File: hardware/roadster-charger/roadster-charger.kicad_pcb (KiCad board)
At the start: 4 copper layers, 74.4 x 50.2 mm, 105 parts, among them J1 USB4505-03-0-A, J2 USB4505-03-0-A, J3 54-00166, Q1 CSD19532Q5B, U1 MPM3606AGQV-P, U10 DAC70501ZDQFT, U12 PI3740-00-LGIZ, U2 ESP32-C3-MINI-1, U3 INA168, U4 OPA340NA, U5 FUSB307BMPX, U6 LM75B, U7 LM5050-1, U8 INA168, U9 OPA340NA

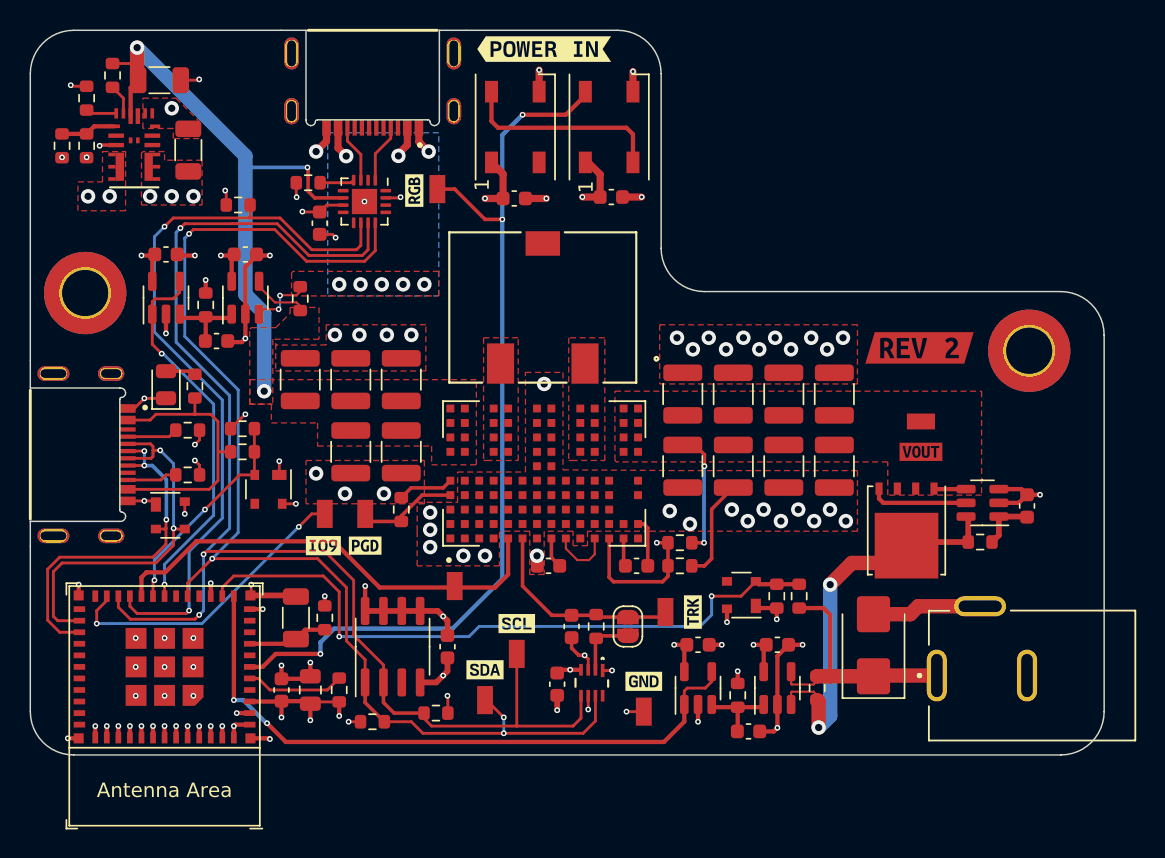
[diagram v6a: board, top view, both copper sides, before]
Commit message: reannotate, add uart test points
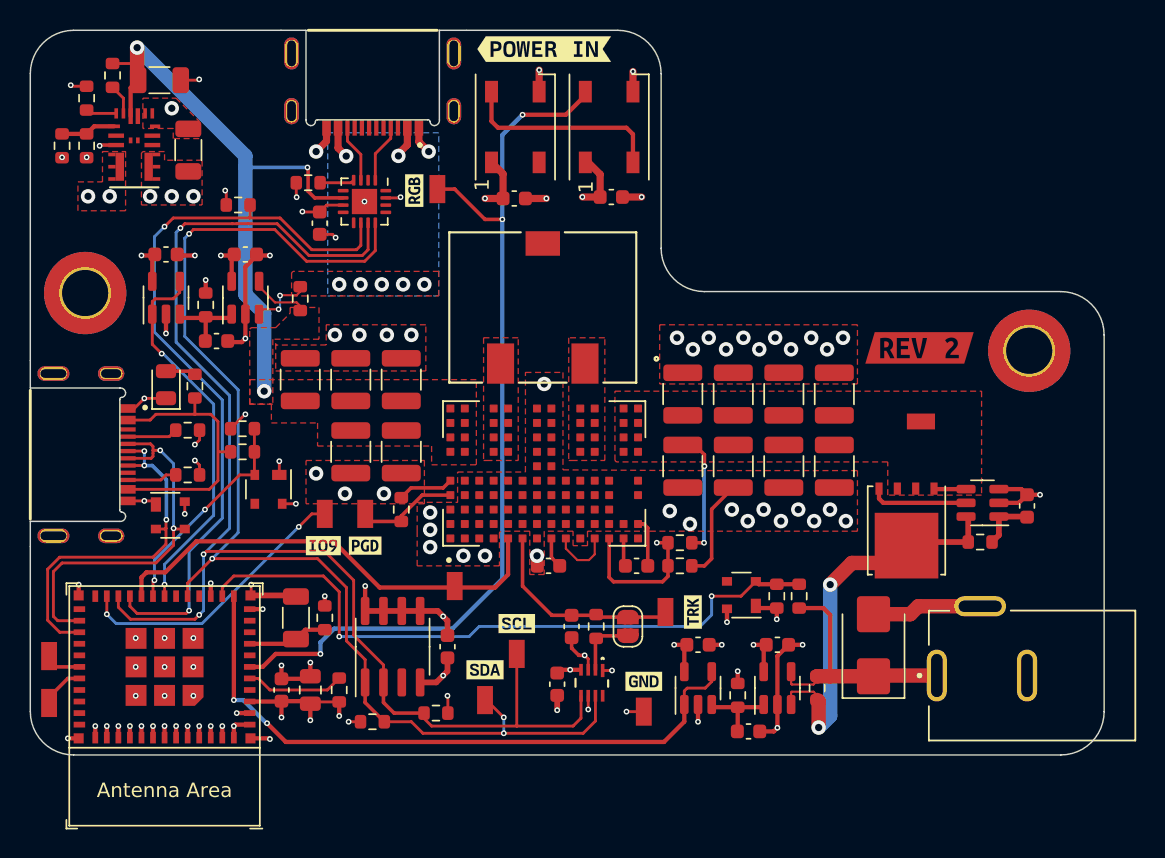
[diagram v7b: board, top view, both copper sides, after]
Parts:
- removed kibuzzard-671EB361: G***, kibuzzard-671EB361
- added TP1: RCU-0C, RCU-0C:TP+195X110, F.Cu at (183.6, 155.9)
- added TP2: RCU-0C, RCU-0C:TP+195X110, F.Cu at (183.6, 152.7)
- added kibuzzard-67218F63: G***, kibuzzard-67218F63, F.Cu at (244.0, 138.5)
- renumbered C25 to C18, C21 to C19, C22 to C20, C23 to C21, C26 to C22, C18 to C23, C20 to C24, C19 to C25, C31 to C26, C32 to C27, C33 to C28, C24 to C29, C27 to C30, C28 to C31, C29 to C32, C30 to C33, D7 to D4, D4 to D5, D5 to D7, R22 to R20, R20 to R21, R21 to R22, R25 to R23, R26 to R25, R23 to R26, TP6 to TP10, TP9 to TP11, TP1 to TP3, TP2 to TP4, TP3 to TP5, TP4 to TP6, TP5 to TP7, TP7 to TP9, U12 to U11
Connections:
- U2 pad 30: unconnected-(U2-GPIO20/U0RXD-Pad30) -> /U0_RX
- U2 pad 31: unconnected-(U2-GPIO21/U0TXD-Pad31) -> /U0_TX
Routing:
- net /U0_TX: track 0.00 -> 3.04 mm
- net /U0_RX: track 0.00 -> 2.67 mm
- net /IO9_BOOT: track 21.1 -> 19.8 mm

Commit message: use track cleanup tool
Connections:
- J1 pad S1: GND -> unconnected-(J1-SHELL_GND-PadS1)_1
- J1 pad S2: GND -> unconnected-(J1-SHELL_GND-PadS1)_3
- J1 pad S3: GND -> unconnected-(J1-SHELL_GND-PadS1)
- J1 pad S4: GND -> unconnected-(J1-SHELL_GND-PadS1)_2
- J2 pad S1: GND -> unconnected-(J2-SHELL_GND-PadS1)_1
- J2 pad S2: GND -> unconnected-(J2-SHELL_GND-PadS1)_2
- J2 pad S3: GND -> unconnected-(J2-SHELL_GND-PadS1)_3
- J2 pad S4: GND -> unconnected-(J2-SHELL_GND-PadS1)
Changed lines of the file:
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@@
 	(net 91 "Net-(U11-VDIFF)")
 	(net 92 "unconnected-(U11-SYNCO-PadC1)")
+	(net 93 "unconnected-(J1-SHELL_GND-PadS1)")
+	(net 94 "unconnected-(J1-SHELL_GND-PadS1)_1")
+	(net 95 "unconnected-(J1-SHELL_GND-PadS1)_2")
+	(net 96 "unconnected-(J1-SHELL_GND-PadS1)_3")
+	(net 97 "unconnected-(J2-SHELL_GND-PadS1)")
+	(net 98 "unconnected-(J2-SHELL_GND-PadS1)_1")
+	(net 99 "unconnected-(J2-SHELL_GND-PadS1)_2")
+	(net 100 "unconnected-(J2-SHELL_GND-PadS1)_3")
 	(footprint "kibuzzard-657BB005"
 		(layer "F.Cu")
@@
 			(layers "*.Cu")
 			(remove_unused_layers no)
-			(net 2 "GND")
+			(net 98 "unconnected-(J2-SHELL_GND-PadS1)_1")
 			(pinfunction "SHELL_GND")
-			(pintype "power_in")
+			(pintype "power_in+no_connect")
 		)
 		(pad "S2" thru_hole oval
@@
 			(layers "*.Cu")
 			(remove_unused_layers no)
-			(net 2 "GND")
+			(net 99 "unconnected-(J2-SHELL_GND-PadS1)_2")
 			(pinfunction "SHELL_GND")
-			(pintype "power_in")
+			(pintype "power_in+no_connect")
 		)
 		(pad "S3" thru_hole oval
@@
 			(layers "*.Cu")
 			(remove_unused_layers no)
-			(net 2 "GND")
+			(net 100 "unconnected-(J2-SHELL_GND-PadS1)_3")
 			(pinfunction "SHELL_GND")
-			(pintype "power_in")
+			(pintype "power_in+no_connect")
 		)
 		(pad "S4" thru_hole oval
@@
 			(layers "*.Cu")
 			(remove_unused_layers no)
-			(net 2 "GND")
+			(net 97 "unconnected-(J2-SHELL_GND-PadS1)")
 			(pinfunction "SHELL_GND")
-			(pintype "power_in")
+			(pintype "power_in+no_connect")
 		)
 		(model "${KIPRJMOD}/components/USB4505-03-0-A_REVA/USB4505-03-0-A_REVA.step"
@@
 			(layers "*.Cu")
 			(remove_unused_layers no)
-			(net 2 "GND")
+			(net 94 "unconnected-(J1-SHELL_GND-PadS1)_1")
 			(pinfunction "SHELL_GND")
-			(pintype "power_in")
+			(pintype "power_in+no_connect")
 		)
 		(pad "S2" thru_hole oval
@@
 			(layers "*.Cu")
 			(remove_unused_layers no)
-			(net 2 "GND")
+			(net 96 "unconnected-(J1-SHELL_GND-PadS1)_3")
 			(pinfunction "SHELL_GND")
-			(pintype "power_in")
+			(pintype "power_in+no_connect")
 		)
 		(pad "S3" thru_hole oval
@@
 			(layers "*.Cu")
 			(remove_unused_layers no)
-			(net 2 "GND")
+			(net 93 "unconnected-(J1-SHELL_GND-PadS1)")
 			(pinfunction "SHELL_GND")
-			(pintype "power_in")
+			(pintype "power_in+no_connect")
 		)
 		(pad "S4" thru_hole oval
@@
 			(layers "*.Cu")
 			(remove_unused_layers no)
-			(net 2 "GND")
+			(net 95 "unconnected-(J1-SHELL_GND-PadS1)_2")
 			(pinfunction "SHELL_GND")
-			(pintype "power_in")
+			(pintype "power_in+no_connect")
 		)
 		(model "${KIPRJMOD}/components/USB4505-03-0-A_REVA/USB4505-03-0-A_REVA.step"
@@
 				(font
 					(size 0.001 0.001)
+					(thickness 0.15)
 				)
 			)
@@
 				(font
 					(size 0.001 0.001)
+					(thickness 0.15)
 				)
 			)
@@
 	)
 	(segment
-		(start 186.75 158.35)
-		(end 186.8 158.3)
-		(width 0.2)
-		(layer "F.Cu")
-		(net 2)
-	)
-	(segment
 		(start 190 158.3)
 		(end 190 157.5)
@@
 	)
 	(segment
-		(start 204.5 157.2)
-		(end 204.45 157.2)
-		(width 0.2)
-		(layer "F.Cu")
-		(net 3)
-	)
-	(segment
 		(start 190 124.9)
 		(end 190.575 124.9)
@@
 	)
 	(segment
-		(start 194.45 130.875)
-		(end 194.425 130.9)
-		(width 0.3)
-		(layer "F.Cu")
-		(net 5)
-	)
-	(segment
 		(start 194.45 129.225)
 		(end 196.0625 129.225)
@@
 	)
 	(segment
-		(start 190.2 139)
-		(end 190.2 139.4495)
-		(width 0.2)
-		(layer "B.Cu")
-		(net 18)
-	)
-	(segment
 		(start 190.7495 139.4495)
 		(end 190.2 139.4495)
@@
 	(segment
 		(start 190.2 138.4495)
-		(end 190.2 139)
+		(end 190.2 139.4495)
 		(width 0.2)
 		(layer "B.Cu")
@@
 	)
 	(segment
-		(start 190.8 138.6)
+		(start 190.8 138.4)
 		(end 190.8 138.82)
 		(width 0.2)
@@
 	)
 	(segment
-		(start 190.8 138.4)
-		(end 190.8 138.6)
-		(width 0.2)
-		(layer "F.Cu")
-		(net 19)
-	)
-	(segment
 		(start 190.63 137.95)
 		(end 190.8 138.12)
@@
 	)
 	(segment
-		(start 198.1245 128.6245)
-		(end 198.1 128.6)
-		(width 0.15)
-		(layer "F.Cu")
-		(net 24)
-	)
-	(segment
 		(start 200.75 127.65)
 		(end 199.6255 127.65)
@@
 	)
 	(segment
-		(start 199.399999 122.7)
-		(end 197.4 122.7)
+		(start 193 122.7)
+		(end 199.399999 122.7)
 		(width 0.2)
 		(layer "F.Cu")
@@
 	)
 	(segment
-		(start 196.6 122.7)
-		(end 196.3 122.7)
-		(width 0.2)
-		(layer "F.Cu")
-		(net 45)
-	)
-	(segment
 		(start 204.7 147.4)
 		(end 204.7 151.2)
@@
 	)
 	(segment
-		(start 197.4 122.7)
-		(end 196.6 122.7)
-		(width 0.2)
-		(layer "F.Cu")
-		(net 45)
-	)
-	(segment
 		(start 207.5 156.6)
 		(end 209.575 156.6)
@@
 	)
 	(segment
-		(start 196.3 122.7)
-		(end 193 122.7)
-		(width 0.2)
-		(layer "F.Cu")
-		(net 45)
-	)
-	(segment
 		(start 205.3 124.9)
 		(end 201.6 124.9)
@@
 		(width 0.25)
 		(layer "F.Cu")
-		(net 90)
-	)
-	(segment
-		(start 219.85 149.775)
-		(end 219.8 149.825)
-		(width 0.25)
-		(layer "F.Cu")
